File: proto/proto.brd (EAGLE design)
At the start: 33.3 x 33.3 mm, 3 parts

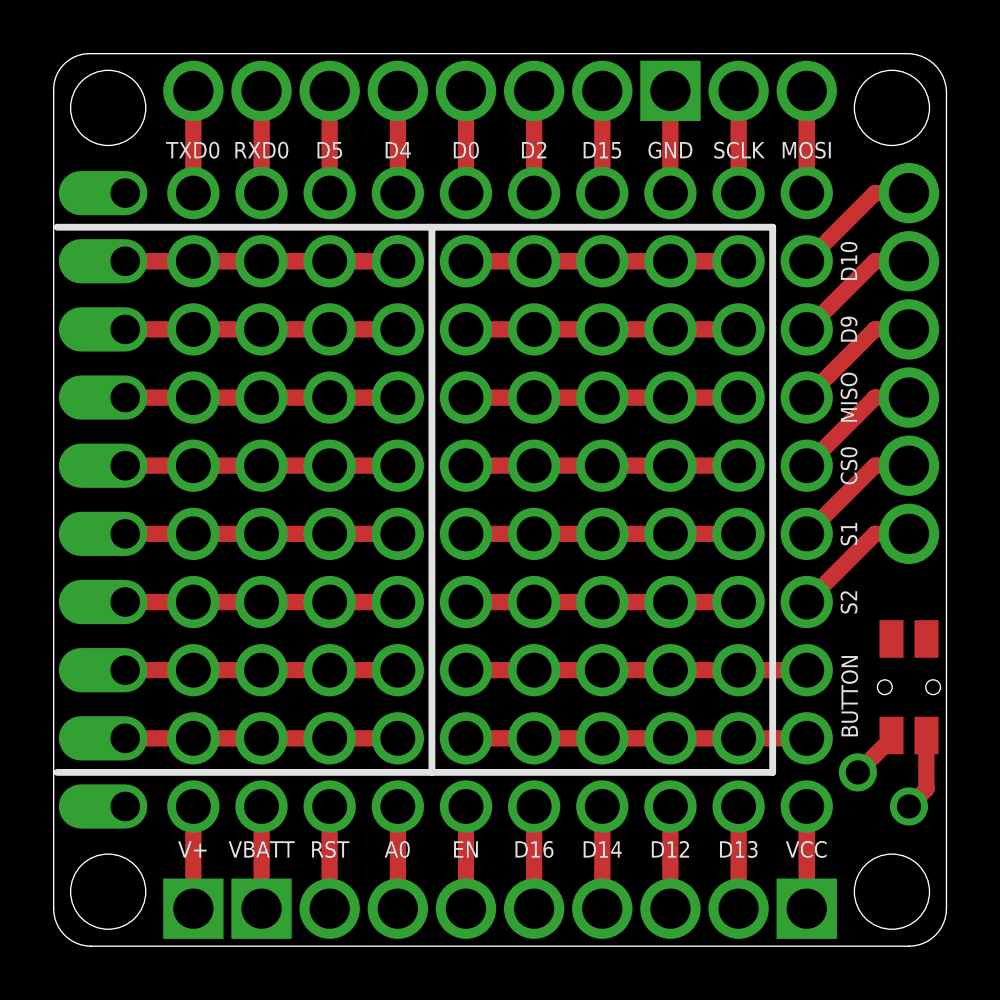
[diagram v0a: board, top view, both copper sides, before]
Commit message: Unify all boards, buttons in the same place, board dimension reduced to 1.32inch
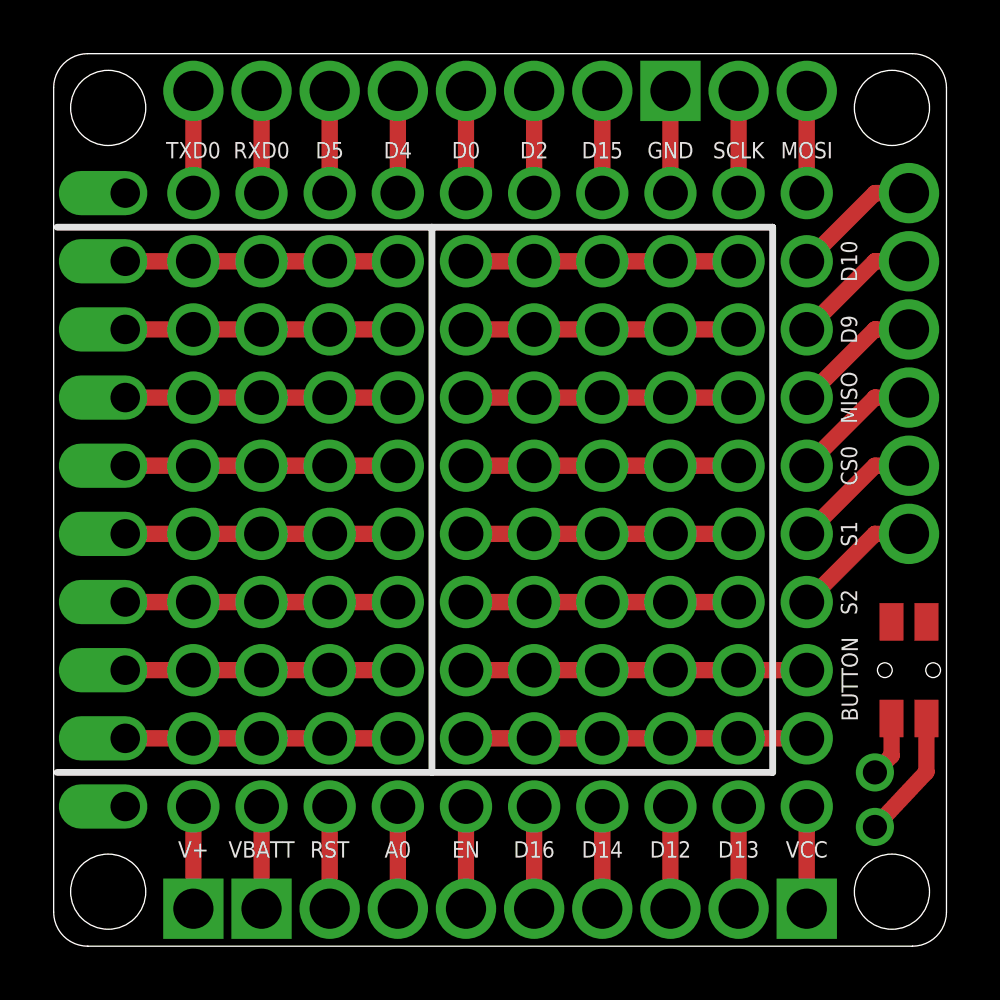
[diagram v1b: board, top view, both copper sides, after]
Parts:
- moved BUTTON 0.63 mm to (33.0, 11.4)
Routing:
- net SW2: track 2.91 -> 4.80 mm
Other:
- outline, holes or cut-outs redrawn
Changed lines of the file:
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@@
 <board>
 <plain>
-<wire x1="32.8932" y1="34.407" x2="2.413" y2="34.407" width="0" layer="20"/>
-<wire x1="2.413" y1="34.407" x2="1.143" y2="33.01" width="0" layer="20" curve="90"/>
-<wire x1="1.143" y1="33.01" x2="1.143" y2="2.54" width="0" layer="20"/>
-<wire x1="1.143" y1="2.54" x2="2.54" y2="1.143" width="0" layer="20" curve="90"/>
-<wire x1="2.54" y1="1.143" x2="33.0202" y2="1.143" width="0" layer="20"/>
-<wire x1="33.0202" y1="1.143" x2="34.4172" y2="2.54" width="0" layer="20" curve="90"/>
-<wire x1="34.4172" y1="2.54" x2="34.4172" y2="33.01" width="0" layer="20"/>
-<wire x1="34.4172" y1="33.01" x2="32.8932" y2="34.407" width="0" layer="20" curve="90"/>
+<wire x1="1.143" y1="33.137" x2="1.143" y2="2.413" width="0" layer="20"/>
+<wire x1="1.143" y1="2.413" x2="2.413" y2="1.143" width="0" layer="20" curve="90"/>
+<wire x1="2.413" y1="1.143" x2="33.1472" y2="1.143" width="0" layer="20"/>
+<wire x1="33.1472" y1="1.143" x2="34.4172" y2="2.413" width="0" layer="20" curve="90"/>
+<wire x1="34.4172" y1="2.413" x2="34.4172" y2="33.137" width="0" layer="20"/>
+<wire x1="34.4172" y1="33.137" x2="33.1472" y2="34.407" width="0" layer="20" curve="90"/>
+<wire x1="33.1472" y1="34.407" x2="2.413" y2="34.407" width="0" layer="20"/>
+<wire x1="2.413" y1="34.407" x2="1.143" y2="33.137" width="0" layer="20" curve="90"/>
 <text x="6.35" y="31.115" size="0.6096" layer="21" align="top-center">TXD0</text>
 <text x="8.89" y="31.115" size="0.6096" layer="21" align="top-center">RXD0</text>
@@
 <elements>
 <element name="H1" library="ESPstack" package="ESP-BOARD" value="ESP-BOARD" x="24.13" y="19.05"/>
-<element name="BUTTON" library="ESPstack" package="SKSCLDE010" value="" x="33.02" y="10.795" smashed="yes" rot="R90">
-<attribute name="NAME" x="31.115" y="8.89" size="0.6096" layer="25" rot="R90"/>
-<attribute name="VALUE" x="36.83" y="8.255" size="1.27" layer="27" rot="R90"/>
+<element name="BUTTON" library="ESPstack" package="SKSCLDE010" value="" x="33.02" y="11.43" smashed="yes" rot="R90">
+<attribute name="NAME" x="31.115" y="9.525" size="0.6096" layer="25" rot="R90"/>
+<attribute name="VALUE" x="36.83" y="8.89" size="1.27" layer="27" rot="R90"/>
 </element>
 <element name="U$1" library="ESPstack" package="1X10-EDGE" value="1X10-EDGE" x="3.81" y="17.78"/>
@@
 </signal>
 <signal name="SW2">
-<via x="33.02" y="6.35" extent="1-16" drill="0.9" diameter="1.4224"/>
+<via x="31.75" y="5.588" extent="1-16" drill="0.9" diameter="1.4224"/>
 <contactref element="BUTTON" pad="1"/>
 <contactref element="BUTTON" pad="2"/>
-<wire x1="33.67" y1="12.595" x2="33.67" y2="8.995" width="0" layer="19" extent="1-16"/>
-<wire x1="33.02" y1="6.35" x2="33.67" y2="7" width="0.6096" layer="1"/>
-<wire x1="33.67" y1="7" x2="33.67" y2="8.995" width="0.6096" layer="1"/>
+<wire x1="33.67" y1="13.23" x2="33.67" y2="9.63" width="0" layer="19" extent="1-16"/>
+<wire x1="31.75" y1="5.588" x2="33.67" y2="7.635" width="0.6096" layer="1"/>
+<wire x1="33.67" y1="7.635" x2="33.67" y2="9.63" width="0.6096" layer="1"/>
 </signal>
 <signal name="SW1">
-<via x="31.115" y="7.62" extent="1-16" drill="0.9" diameter="1.4224"/>
+<via x="31.75" y="7.62" extent="1-16" drill="0.9" diameter="1.4224"/>
 <contactref element="BUTTON" pad="3"/>
 <contactref element="BUTTON" pad="4"/>
-<wire x1="32.37" y1="12.595" x2="32.37" y2="8.995" width="0" layer="19" extent="1-16"/>
-<wire x1="31.115" y1="7.62" x2="32.37" y2="8.875" width="0.6096" layer="1"/>
-<wire x1="32.37" y1="8.875" x2="32.37" y2="8.995" width="0.6096" layer="1"/>
+<wire x1="32.37" y1="13.23" x2="32.37" y2="9.63" width="0" layer="19" extent="1-16"/>
+<wire x1="31.75" y1="7.62" x2="32.37" y2="8.24" width="0.6096" layer="1"/>
+<wire x1="32.37" y1="8.24" x2="32.37" y2="9.63" width="0.6096" layer="1"/>
 </signal>
 <signal name="P9">
